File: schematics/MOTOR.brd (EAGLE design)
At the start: 76 x 76 mm, 79 parts

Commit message: фцыувкаепнргошщз
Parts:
- BUT1, BUT2, BUT3, BUT4, BUT5, BUT6, BUT7: device pinhead:1X02 -> pinheadCS:1X02
- MOT1, MOT2, MOT3, MOT4, MOT5, MOT6, MOT7: value (none) -> JST-2-2.5; device pinhead:1X02 -> UNKNOWN-2024:JST-2-2.5
- moved MOT5 253.2 mm to (-1.25, -177.3)
- moved MOT6 249.9 mm to (-1.25, -190.0)
- moved MOT4 239.2 mm to (-1.25, -164.6)
- moved MOT7 235.8 mm to (-1.25, -202.7)
- moved MOT3 212.6 mm to (-1.25, -151.9), turned to 0 degrees
- moved BUT4 194.8 mm to (-1.27, -113.8), turned to 0 degrees
- moved BUT5 180.0 mm to (-1.27, -101.1), turned to 0 degrees
- moved MOT2 170.3 mm to (-1.25, -139.2), turned to 0 degrees
- moved BUT6 150.2 mm to (-1.27, -88.4), turned to 0 degrees
- moved MOT1 142.4 mm to (-1.25, -126.5), turned to 0 degrees
- moved BUT3 129.8 mm to (-1.27, -63.0), turned to 0 degrees
- moved BUT7 112.1 mm to (-1.27, -75.7), turned to 0 degrees
- moved BUT2 90.4 mm to (-1.27, -50.3), turned to 0 degrees
- moved BUT1 54.0 mm to (-1.27, -37.6), turned to 0 degrees

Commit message: компоненты внутри рабочей области
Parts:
- moved MOT5 255.8 mm to (50.5, 73.2)
- moved MOT6 252.2 mm to (66.0, 53.1)
- moved MOT7 241.8 mm to (68.5, 28.8)
- moved MOT4 238.7 mm to (27.9, 72.3)
- moved MOT3 205.2 mm to (10.2, 53.0)
- moved MOT2 170.9 mm to (11.6, 31.2)
- moved BUT6 168.3 mm to (65.1, 66.3)
- moved BUT5 161.1 mm to (76.1, 40.2)
- moved BUT7 157.6 mm to (40.0, 76.4)
- moved BUT4 144.4 mm to (65.6, 14.2)
- moved MOT1 139.6 mm to (22.8, 11.0)
- moved BUT3 129.8 mm to (15.8, 65.7)
- moved JP19 108.6 mm to (101.3, 38.1)
- moved JP2 104.2 mm to (101.8, 54.2)
- moved JP1 104.2 mm to (101.0, 66.2)
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
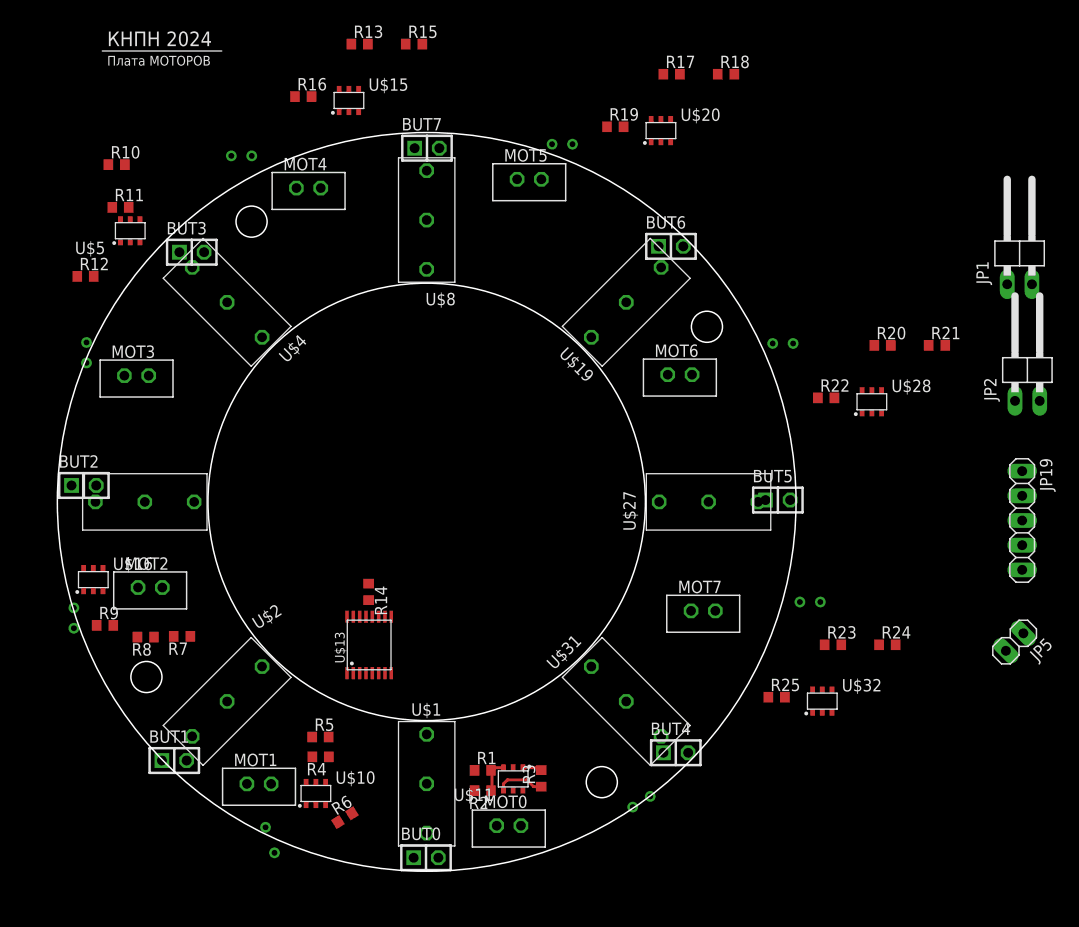
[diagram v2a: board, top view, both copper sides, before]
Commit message: Плата MOTOR разведена, но не сделана шелкография
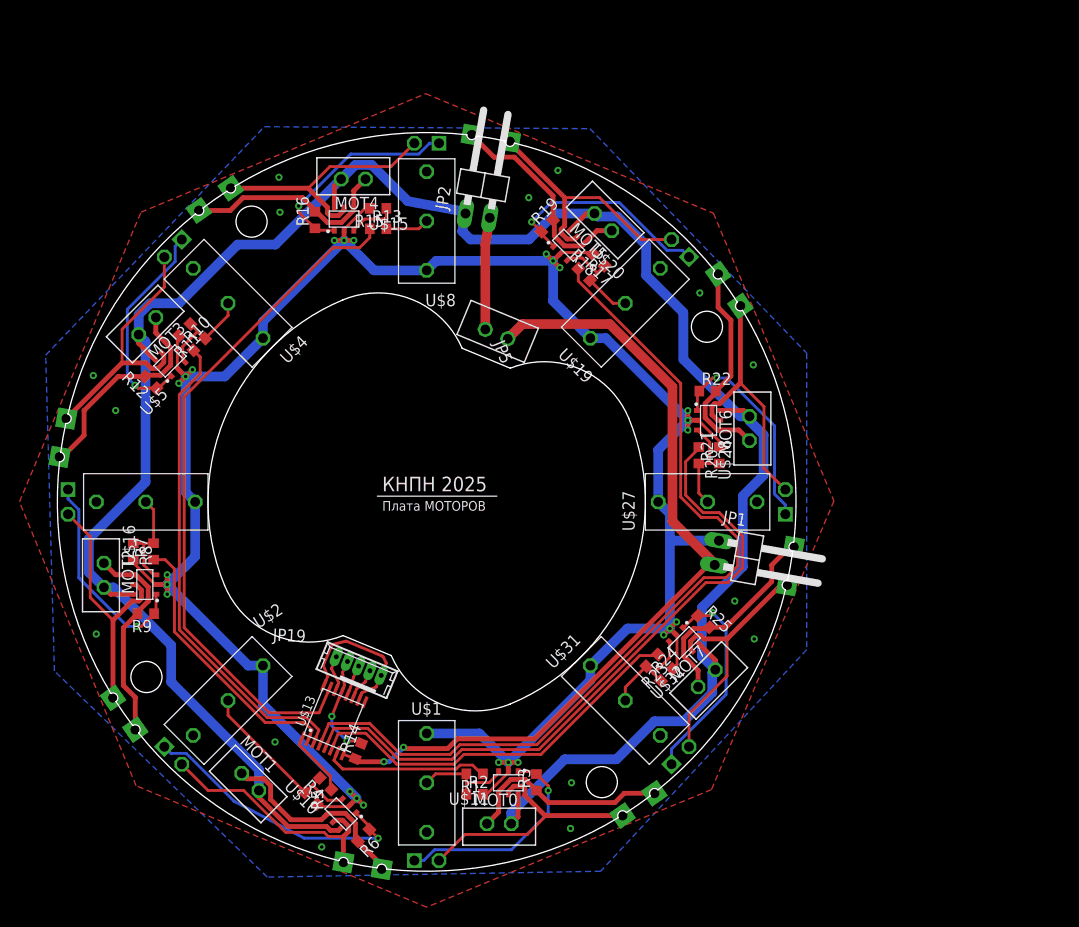
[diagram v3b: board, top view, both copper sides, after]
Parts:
- removed U$12, U$17, U$21, U$23, U$25, U$29, U$33, U$6: -, NA-2025:VIAS
- removed U$14, U$18, U$22, U$24, U$26, U$30, U$34, U$7: +, NA-2025:VIAS
- added U$35, U$36, U$37, U$38, U$39, U$40, U$41, U$42: CONTACT_SIDE_4MM_2PIN, UNKNOWN-2024:CONTACT_SIDE_4MM_2PIN
- JP19: value (none) -> MOLEX-5-1.25; device pinhead:1X05 -> UNKNOWN-2024:53047-05
- JP5: value (none) -> JST-2-2.5; device pinhead:1X02 -> UNKNOWN-2024:JST-2-2.5
- moved JP19 70.1 mm to (32.8, 22.7), turned to 337.5 degrees
- moved BUT4 67.7 mm to (40.0, 76.9), flipped to the bottom
- moved BUT7 67.7 mm to (66.1, 13.9), flipped to the bottom, turned to 135 degrees
- moved JP5 62.0 mm to (47.2, 57.3), turned to 157.5 degrees
- moved JP2 59.0 mm to (45.9, 73.2), turned to 350 degrees
- moved U$9 53.8 mm to (34.9, 40.6)
- moved JP1 42.2 mm to (73.6, 34.1), turned to 260 degrees
- moved BUT6 28.8 mm to (76.9, 40.0), flipped to the bottom, turned to 90 degrees
- moved BUT5 27.8 mm to (66.1, 66.1), flipped to the bottom, turned to 45 degrees
- moved R21 25.1 mm to (70.1, 44.8), turned to 90 degrees
- moved R18 23.2 mm to (57.7, 64.9), turned to 135 degrees
- moved R24 22.9 mm to (64.7, 22.2), turned to 45 degrees
- moved R17 22.5 mm to (56.2, 63.4), turned to 315 degrees
- moved R20 22.0 mm to (68.0, 44.8), turned to 270 degrees
- moved R10 20.4 mm to (16.6, 56.2), turned to 45 degrees
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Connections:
- net MOTOR0: now also U$13.7; no longer U$13.15
- net MOTOR4: now also U$13.15; no longer U$13.4
- net MOTOR5: now also U$13.4; no longer U$13.5
- net MOTOR6: now also U$13.5; no longer U$13.6
- net MOTOR7: now also U$13.6; no longer U$13.7
- net N$1: now also U$38.P$1; no longer U$14.P$1
- net N$10: now also U$36.P$2; no longer U$23.P$1
- net N$14: now also U$37.P$1; no longer U$7.P$1
- net N$15: now also U$37.P$2; no longer U$6.P$1
- net N$18: now also U$39.P$1; no longer U$18.P$1
- net N$19: now also U$39.P$2; no longer U$17.P$1
- net N$2: now also U$35.P$1; no longer U$22.P$1
- net N$22: now also U$40.P$1; no longer U$26.P$1
- net N$23: now also U$40.P$2; no longer U$25.P$1
- net N$26: now also U$41.P$1; no longer U$30.P$1
- net N$27: now also U$41.P$2; no longer U$29.P$1
- net N$30: now also U$42.P$1; no longer U$34.P$1
- net N$31: now also U$42.P$2; no longer U$33.P$1
- net N$5: now also U$35.P$2; no longer U$21.P$1
- net N$8: now also U$38.P$2; no longer U$12.P$1
- net N$9: now also U$36.P$1; no longer U$24.P$1
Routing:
- net 16V_IN: track 0.00 -> 240.4 mm
- net GND_IN: track 0.00 -> 237.3 mm, vias 0 -> 39
- net MOTOR5: track 0.00 -> 92.1 mm
- net GND_OUT: track 0.00 -> 87.3 mm, vias 0 -> 2
- net MOTOR4: track 0.00 -> 70.9 mm
- net MOTOR6: track 0.00 -> 70.0 mm
- net MOTOR3: track 0.00 -> 49.9 mm
- net MOTOR7: track 0.00 -> 40.7 mm
- net N$7: track 0.00 -> 28.8 mm, vias 0 -> 1
- net MOTOR2: track 0.00 -> 28.4 mm
- net N$8: track 0.00 -> 26.8 mm
- net N$27: track 0.00 -> 26.6 mm
- net N$15: track 0.00 -> 26.6 mm
- net N$23: track 0.00 -> 26.6 mm
- net N$10: track 0.00 -> 26.6 mm
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- added copper zone on layer 1, net GND_IN
- added copper zone on layer 16, net GND_IN
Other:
- outline, holes or cut-outs redrawn
